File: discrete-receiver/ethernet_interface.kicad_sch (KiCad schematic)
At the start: 6 parts

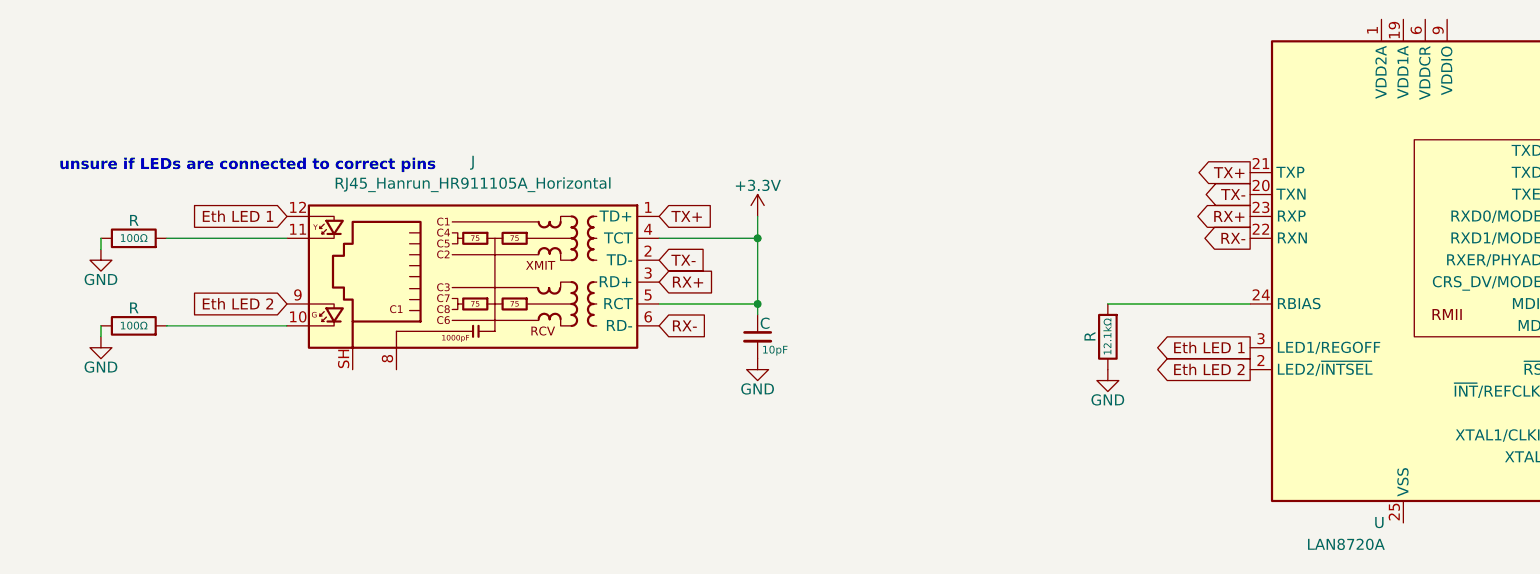
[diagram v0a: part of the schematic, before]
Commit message: updated schematic
clock generator, ADC, and 24.576 oscillator
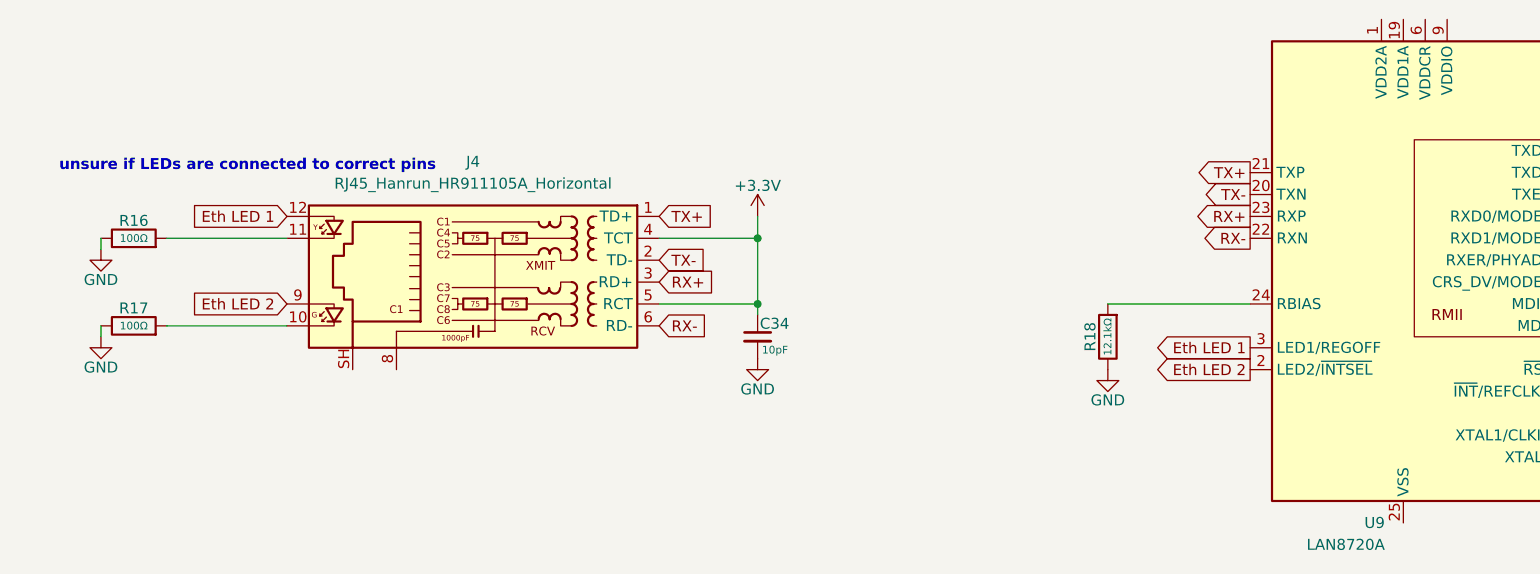
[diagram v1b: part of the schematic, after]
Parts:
- renumbered C to C34, J to J4, R to R16, R to R17, R to R18, U to U9
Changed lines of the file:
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@@
 		(in_pos_files yes)
 		(dnp no)
-		(property "Reference" "R"
+		(property "Reference" "R17"
 			(at 52.07 97.028 90)
 			(show_name no)
@@
 		(instances
 			(project "diode_tayloe_sdr"
-				(path "/d18d178d-3f10-4d68-9036-eae71a7d091a"
+				(path "/d18d178d-3f10-4d68-9036-eae71a7d091a/09065ae7-5d3e-4f86-b983-86dca844c240"
 					(reference "R17")
 					(unit 1)
@@
 		(in_pos_files yes)
 		(dnp no)
-		(property "Reference" "U"
+		(property "Reference" "U9"
 			(at 197.2467 121.92 0)
 			(show_name no)
@@
 		(instances
 			(project "diode_tayloe_sdr"
-				(path "/d18d178d-3f10-4d68-9036-eae71a7d091a"
+				(path "/d18d178d-3f10-4d68-9036-eae71a7d091a/09065ae7-5d3e-4f86-b983-86dca844c240"
 					(reference "U9")
 					(unit 1)
@@
 		(in_pos_files yes)
 		(dnp no)
-		(property "Reference" "#PWR"
+		(property "Reference" "#PWR039"
 			(at 124.46 90.17 0)
 			(hide yes)
@@
 		(instances
 			(project "diode_tayloe_sdr"
-				(path "/d18d178d-3f10-4d68-9036-eae71a7d091a"
+				(path "/d18d178d-3f10-4d68-9036-eae71a7d091a/09065ae7-5d3e-4f86-b983-86dca844c240"
 					(reference "#PWR039")
 					(unit 1)
@@
 		(in_pos_files yes)
 		(dnp no)
-		(property "Reference" "C"
+		(property "Reference" "C34"
 			(at 124.714 98.806 0)
 			(show_name no)
@@
 		(instances
 			(project "diode_tayloe_sdr"
-				(path "/d18d178d-3f10-4d68-9036-eae71a7d091a"
+				(path "/d18d178d-3f10-4d68-9036-eae71a7d091a/09065ae7-5d3e-4f86-b983-86dca844c240"
 					(reference "C34")
 					(unit 1)
@@
 		(in_pos_files yes)
 		(dnp no)
-		(property "Reference" "#PWR"
+		(property "Reference" "#PWR047"
 			(at 124.46 109.22 0)
 			(hide yes)
@@
 		(instances
 			(project "diode_tayloe_sdr"
-				(path "/d18d178d-3f10-4d68-9036-eae71a7d091a"
+				(path "/d18d178d-3f10-4d68-9036-eae71a7d091a/09065ae7-5d3e-4f86-b983-86dca844c240"
 					(reference "#PWR047")
 					(unit 1)
@@
 		(in_pos_files yes)
 		(dnp no)
-		(property "Reference" "R"
+		(property "Reference" "R18"
 			(at 163.068 100.33 90)
 			(show_name no)
@@
 		(instances
 			(project "diode_tayloe_sdr"
-				(path "/d18d178d-3f10-4d68-9036-eae71a7d091a"
+				(path "/d18d178d-3f10-4d68-9036-eae71a7d091a/09065ae7-5d3e-4f86-b983-86dca844c240"
 					(reference "R18")
 					(unit 1)
@@
 		(in_pos_files yes)
 		(dnp no)
-		(property "Reference" "J"
+		(property "Reference" "J4"
 			(at 91.44 80.01 0)
 			(show_name no)
@@
 		(instances
 			(project "diode_tayloe_sdr"
-				(path "/d18d178d-3f10-4d68-9036-eae71a7d091a"
+				(path "/d18d178d-3f10-4d68-9036-eae71a7d091a/09065ae7-5d3e-4f86-b983-86dca844c240"
 					(reference "J4")
 					(unit 1)
@@
 		(in_pos_files yes)
 		(dnp no)
-		(property "Reference" "#PWR"
+		(property "Reference" "#PWR050"
 			(at 165.1 110.49 0)
 			(hide yes)
@@
 		(instances
 			(project "diode_tayloe_sdr"
-				(path "/d18d178d-3f10-4d68-9036-eae71a7d091a"
+				(path "/d18d178d-3f10-4d68-9036-eae71a7d091a/09065ae7-5d3e-4f86-b983-86dca844c240"
 					(reference "#PWR050")
 					(unit 1)
@@
 		(in_pos_files yes)
 		(dnp no)
-		(property "Reference" "#PWR"
+		(property "Reference" "#PWR048"
 			(at 48.26 96.52 0)
 			(hide yes)
@@
 		(instances
 			(project "diode_tayloe_sdr"
-				(path "/d18d178d-3f10-4d68-9036-eae71a7d091a"
+				(path "/d18d178d-3f10-4d68-9036-eae71a7d091a/09065ae7-5d3e-4f86-b983-86dca844c240"
 					(reference "#PWR048")
 					(unit 1)
@@
 		(in_pos_files yes)
 		(dnp no)
-		(property "Reference" "#PWR"
+		(property "Reference" "#PWR049"
 			(at 48.26 106.68 0)
 			(hide yes)
@@
 		(instances
 			(project "diode_tayloe_sdr"
-				(path "/d18d178d-3f10-4d68-9036-eae71a7d091a"
+				(path "/d18d178d-3f10-4d68-9036-eae71a7d091a/09065ae7-5d3e-4f86-b983-86dca844c240"
 					(reference "#PWR049")
 					(unit 1)
@@
 		(in_pos_files yes)
 		(dnp no)
-		(property "Reference" "R"
+		(property "Reference" "R16"
 			(at 52.07 86.868 90)
 			(show_name no)
@@
 		(instances
 			(project "diode_tayloe_sdr"
-				(path "/d18d178d-3f10-4d68-9036-eae71a7d091a"
+				(path "/d18d178d-3f10-4d68-9036-eae71a7d091a/09065ae7-5d3e-4f86-b983-86dca844c240"
 					(reference "R16")
 					(unit 1)

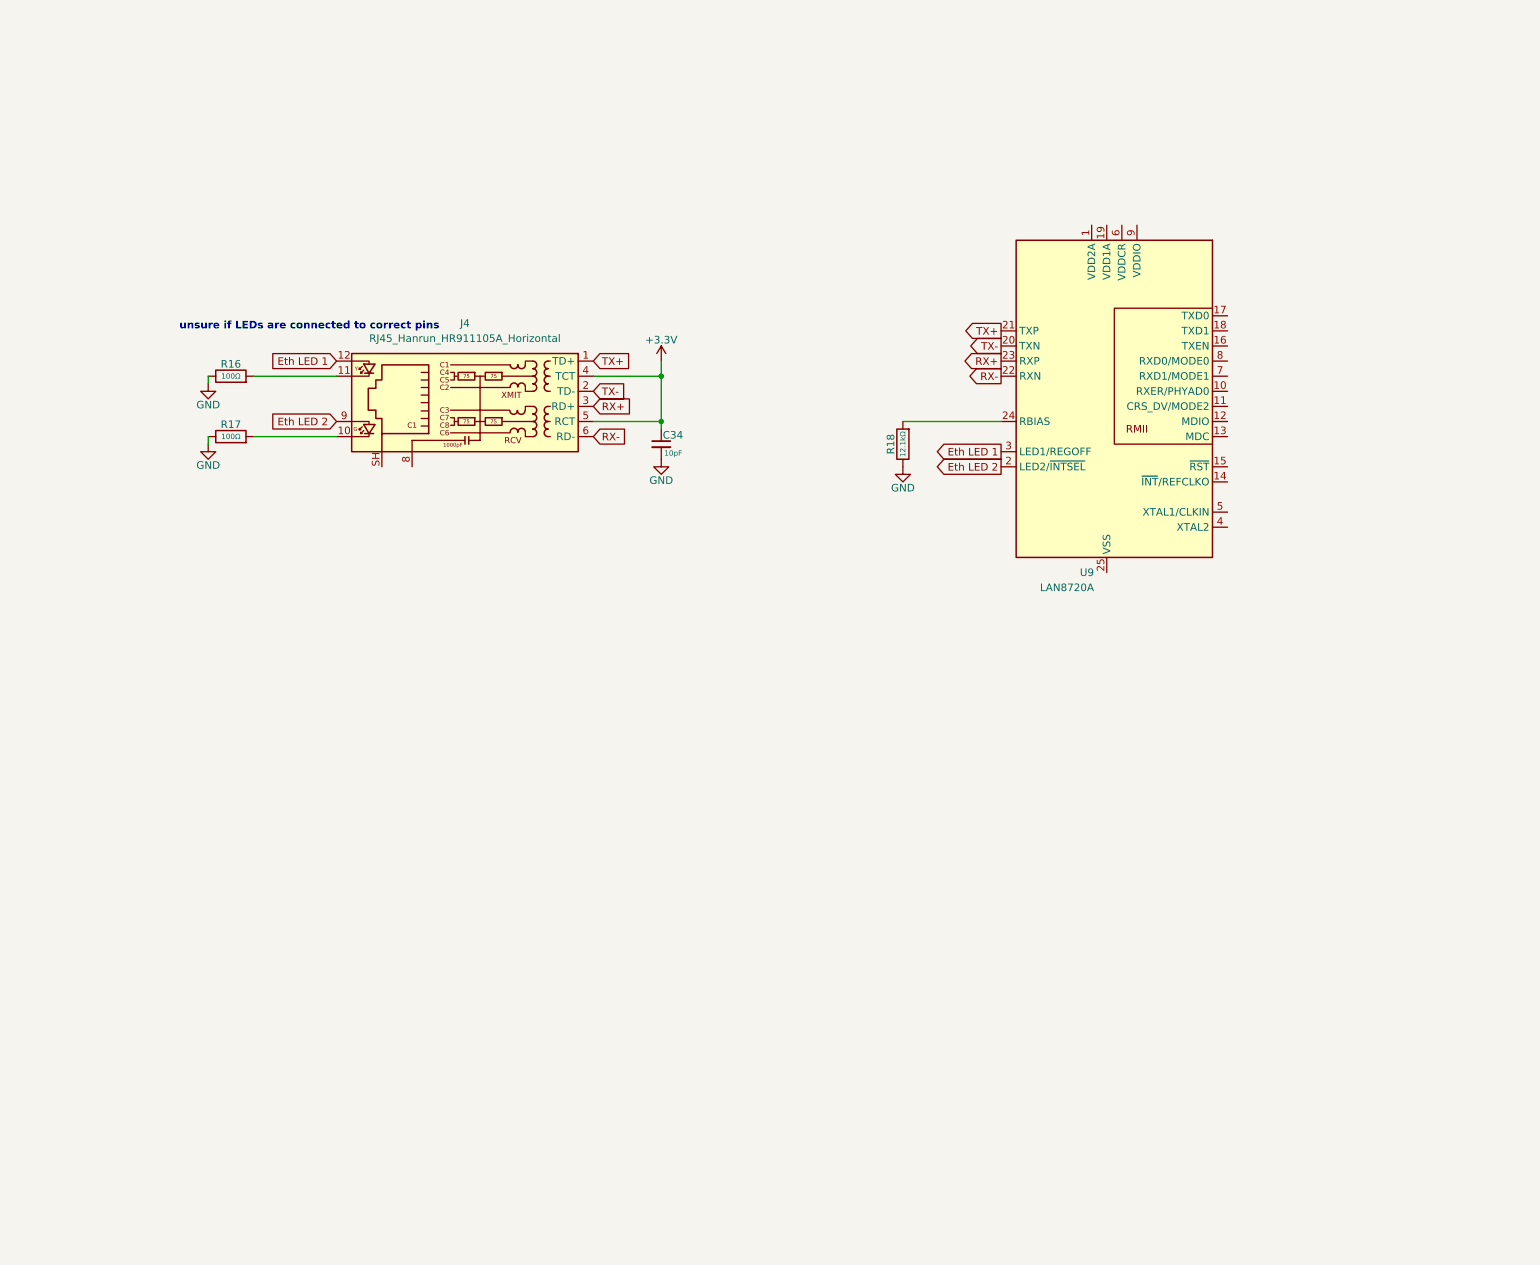
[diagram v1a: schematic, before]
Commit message: POE implemented, working on finishing Ethernet Implementation
I've added the SI-52003 rj45 jack with included magnetics, which is designed for POE and has outputs for such. The 4 power lines pass through two full bridge rectifiers to ensure the polarity of a 48V POE source, then that voltage is fed to an AG9905LP DC-DC converter. This module is designed to be low-noise, although still not perfect. By jumpering its ADJ pin to V- (GND), we can boost it's output voltage to 5.65V rather than 5V. Then, we can use a low-noise LDO regulator to filter the voltage as much as possible to create a good 5V source for the rest of the components on the board. Three LM66100 ICs are used as ideal diodes to select whichever of the three power sources has the highest voltage, and not allow backfeeding into the others. These three 5V power sources are USB, barrel jack, and POE. At this point all power sources pass through the TPS7A20, which is our 5V low-noise LDO regulator. That gives us the main 5V bus.
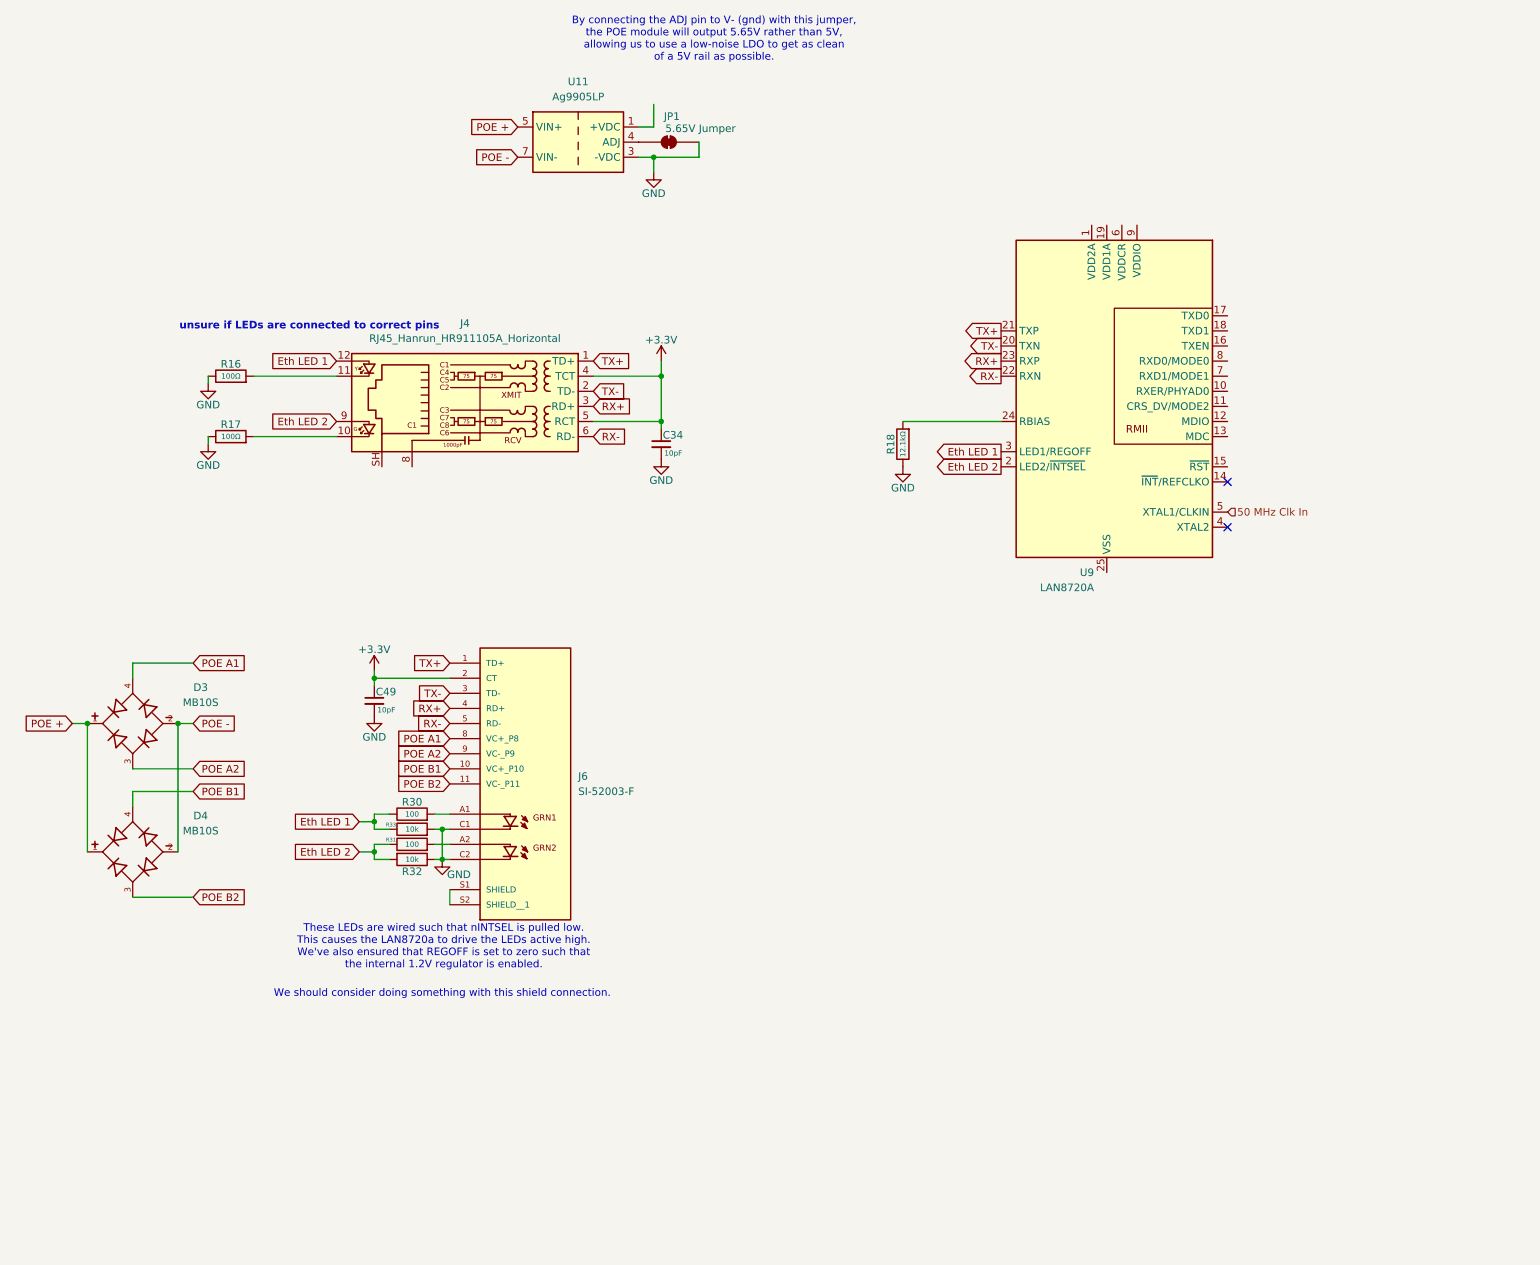
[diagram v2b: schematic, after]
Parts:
- added C49: 10pF, symbol Device:C_Small
- added D3, D4: MB10S, MB10S:SOIC245P670X290-4N, symbol MB10S:MB10S
- added J6: SI-52003-F, SI-52003-F:BEL_SI-52003-F, symbol SI-52003-F:SI-52003-F
- added JP1: 5.65V Jumper, symbol Jumper:SolderJumper_2_Bridged
- added R30, R31: 100, symbol Device:R
- added R32, R33: 10k, symbol Device:R
- added U11: Ag9905LP, Converter_DCDC:Converter_DCDC_Silvertel_Ag99xxLP_THT, symbol Converter_DCDC:Ag9905LP
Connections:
- net +3.3V: now also C49.1, J6.2 (CT)
- net Eth LED 1: now also R30.1, R33.1
- net Eth LED 2: now also R31.1, R32.2
- net GND: now also C49.2, J6.C1, J6.C2, JP1.1 (A), R32.1, R33.2, U11.3 (-VDC)
- net RX+: now also J6.4 (RD+)
- net RX-: now also J6.5 (RD-)
- net TX+: now also J6.1 (TD+)
- net TX-: now also J6.3 (TD-)
- net 50 MHz Clk In: now reaches U9.5 (XTAL1/CLKIN)
- new net: J6.A2, R31.2
- new net: J6.A1, R30.2
- new net: J6.S1 (SHIELD), J6.S2 (SHIELD__1)
- new net: U11.1 (+VDC), U11.2 (+VDC)
- new net: JP1.2 (B), U11.4 (ADJ)
- new net POE +: D3.1, D4.1, U11.5 (VIN+), U11.6 (VIN+)
- new net POE -: D3.2, D4.2, U11.7 (VIN-), U11.8 (VIN-)
- new net POE A1: D3.4, J6.8 (VC+_P8)
- new net POE A2: D3.3, J6.9 (VC-_P9)
- new net POE B1: D4.4, J6.10 (VC+_P10)
- new net POE B2: D4.3, J6.11 (VC-_P11)
- no-connect marks 0 -> 2
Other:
- note added: "By connecting the ADJ pin to V- (gnd) with this jumper, the POE module will output 5.65V rather than 5V, allowing us to use a low-noise LDO to get as clean of a 5V rail as possible."
- note added: "These LEDs are wired such that nINTSEL is pulled low. This causes the LAN8720a to drive the LEDs active high. We've also ensured that REGOFF is set to zero such that the internal 1.2V regulator is enabled."
- note added: "We should consider doing something with this shield connection."
